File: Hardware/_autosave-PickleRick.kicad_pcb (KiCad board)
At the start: 4 copper layers, 100 x 37 mm, 218 parts, among them IC1 TPS259830ONRGER, J1 RBUS, J10 Conn_Coaxial, J11 Conn_Coaxial, J12 Conn_01x03_Male, J13 Conn_01x03_Pin, J14 Conn_01x07_Socket, J2 Conn_01x02_Male, J3 ST1W008S4TR2000, J4 Conn_01x03_Pin, J5 USB_C_Receptacle_USB2.0, J6 Screw_Terminal_01x08, J7 Conn_01x05_Male, J8 DeployLipo, J9 UCLipo, Q1 PMV20ENR, Q10 DMP3099L, Q11 SQS141ELNW-T1_GE3, Q12 SQS141ELNW-T1_GE3, Q2 BUK9M11-40EX, Q3 BUK9M11-40EX, Q4 BUK9M11-40EX, Q5 BUK9M11-40EX, Q8 DMP3099L, Q9 DMP3099L, U1 ESP32-S3, U10 LTC4412xS6, U11 MP28167GQ-A-Z, U14 LTC4412xS6, U16 SC4215, U17 LTC4412xS6, U19 MAX-M10S, U2 DPS368, U20 SN65HVD230, U21 RFM95W-868S2, U22 LTC4412xS6, U3 LTV-247, U4 PCA9534RGVR, U5 PCA9685BS, U6 H3LIS331DLTR, U7 ICM-20608-G, U8 MMC5983MA, U9 LTC4412xS6, Y1 R940000171

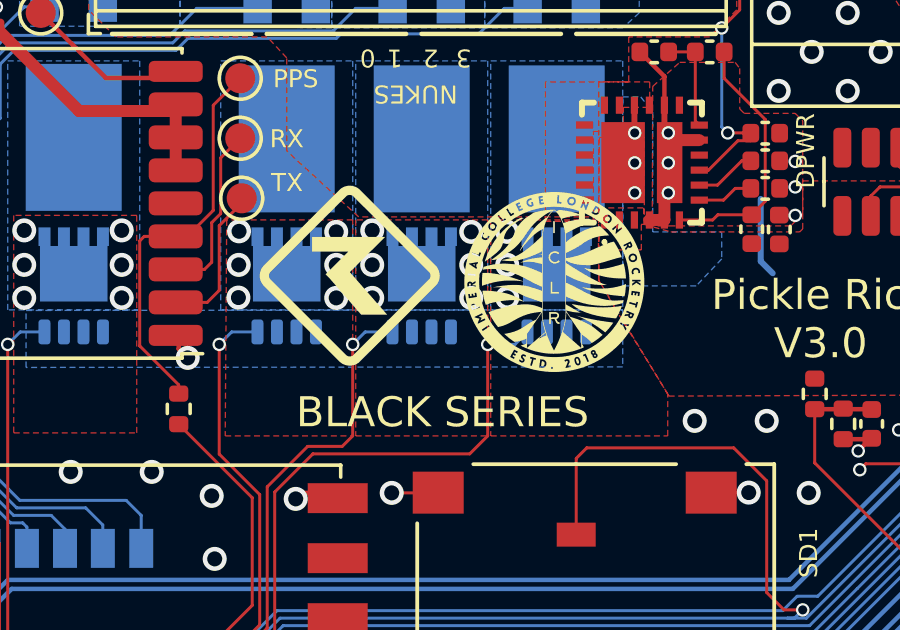
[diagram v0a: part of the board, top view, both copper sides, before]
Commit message: added cont and firing leds
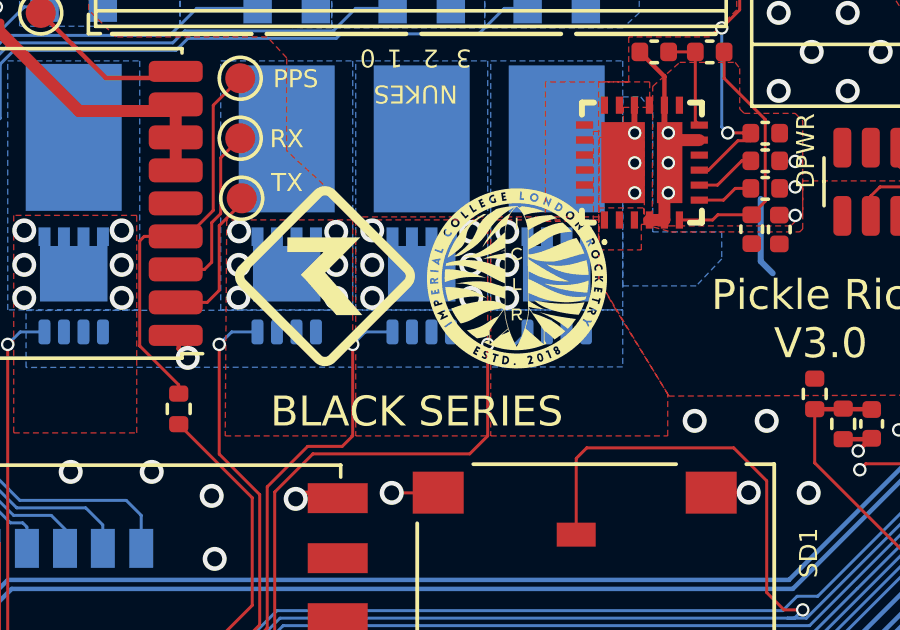
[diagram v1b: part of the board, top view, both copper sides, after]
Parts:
- moved G*** 1.25 mm to (131.9, 74.0)
- moved G*** 0.83 mm to (125.5, 74.0)
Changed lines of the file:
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@@
 	(footprint "iclr-hw:iclr_logo_estd2018_6mm"
 		(layer "F.Cu")
-		(at 133.12 74.17)
+		(at 131.875 74.05)
 		(property "Reference" "G***"
 			(at 0 0 0)
@@
 	(footprint "iclr-hw:rae_logo_6mm"
 		(layer "F.Cu")
-		(at 126.3 73.96)
+		(at 125.475 73.975)
 		(property "Reference" "G***"
 			(at 0 0 0)
@@
 	)
 	(gr_text "BLACK SERIES\n"
-		(at 124.51 79.1 0)
+		(at 123.65 79.075 0)
 		(layer "F.SilkS")
 		(effects
